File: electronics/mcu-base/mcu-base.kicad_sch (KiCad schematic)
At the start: 1 part

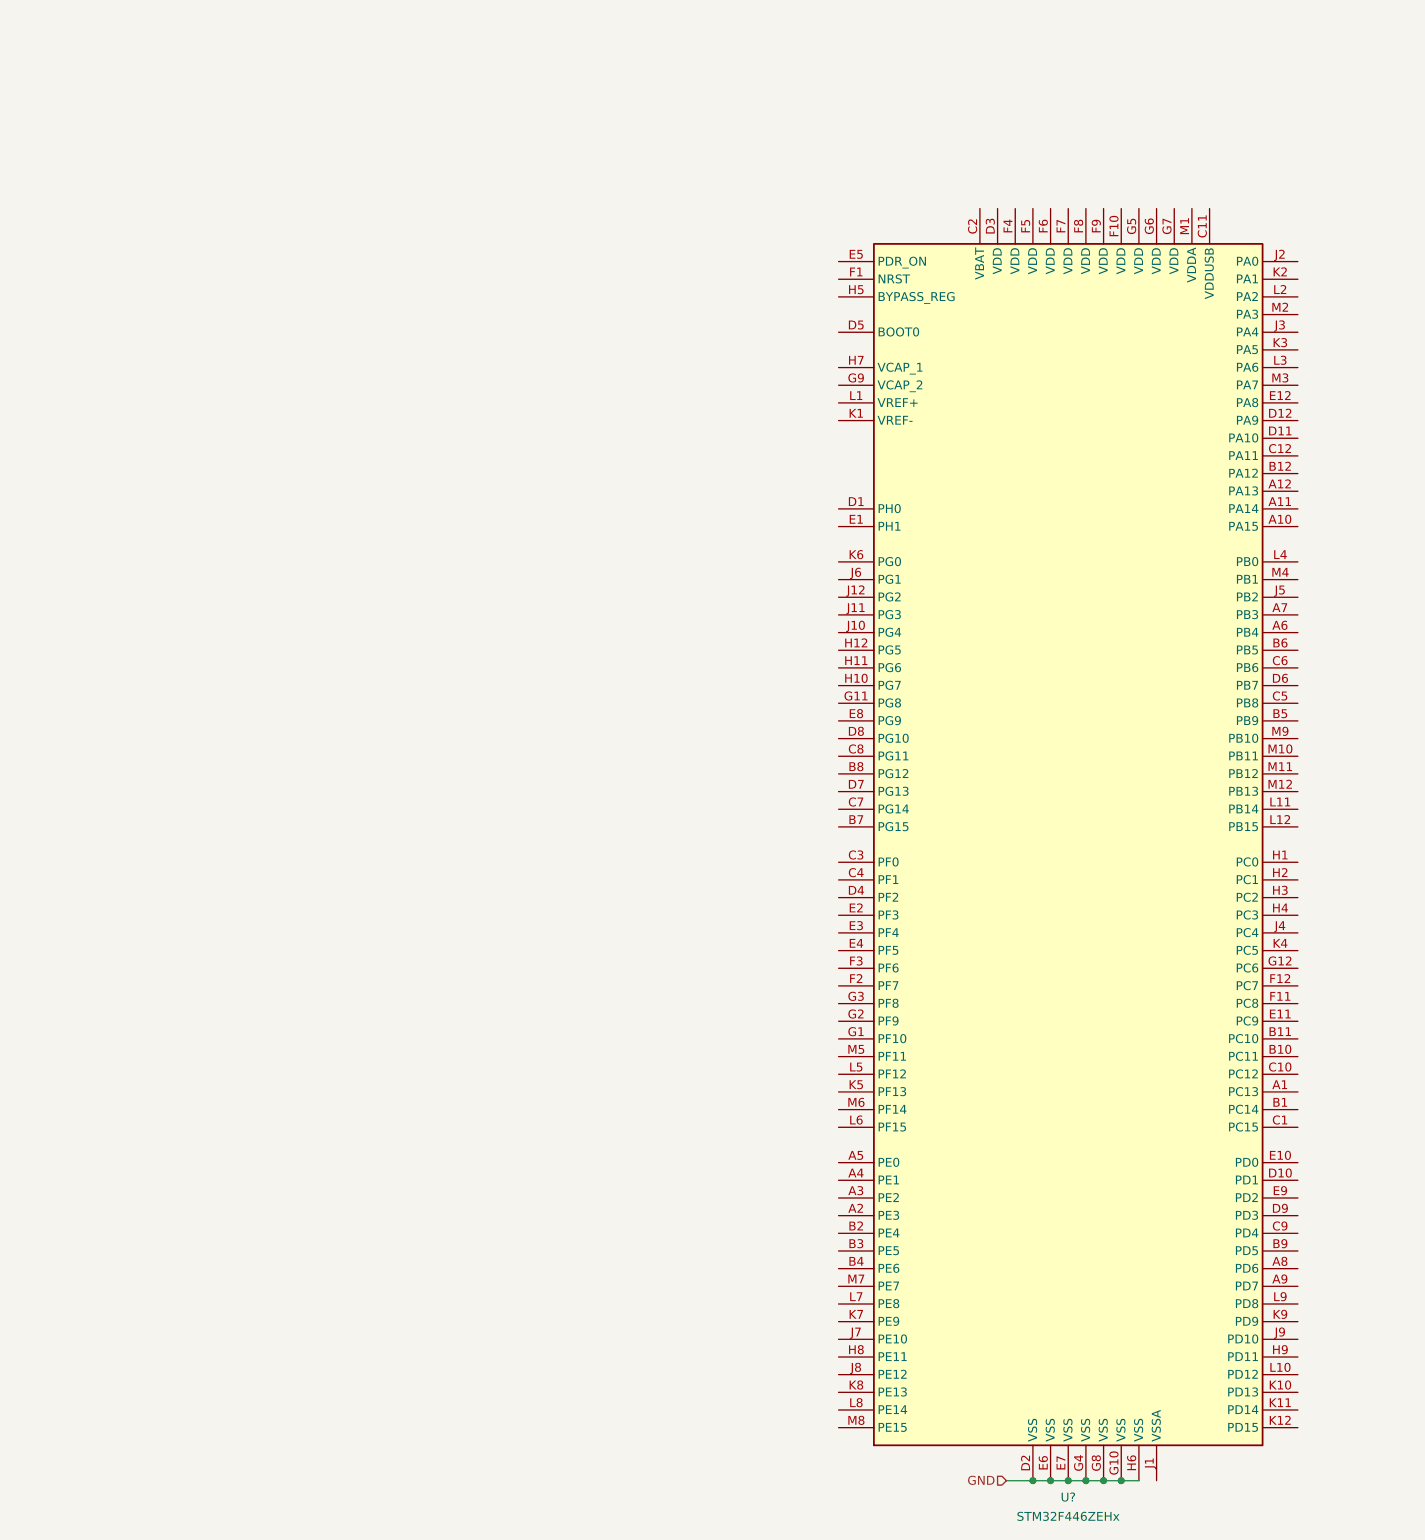
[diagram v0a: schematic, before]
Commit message: Add regulator and CAN transceiver to mcu-base
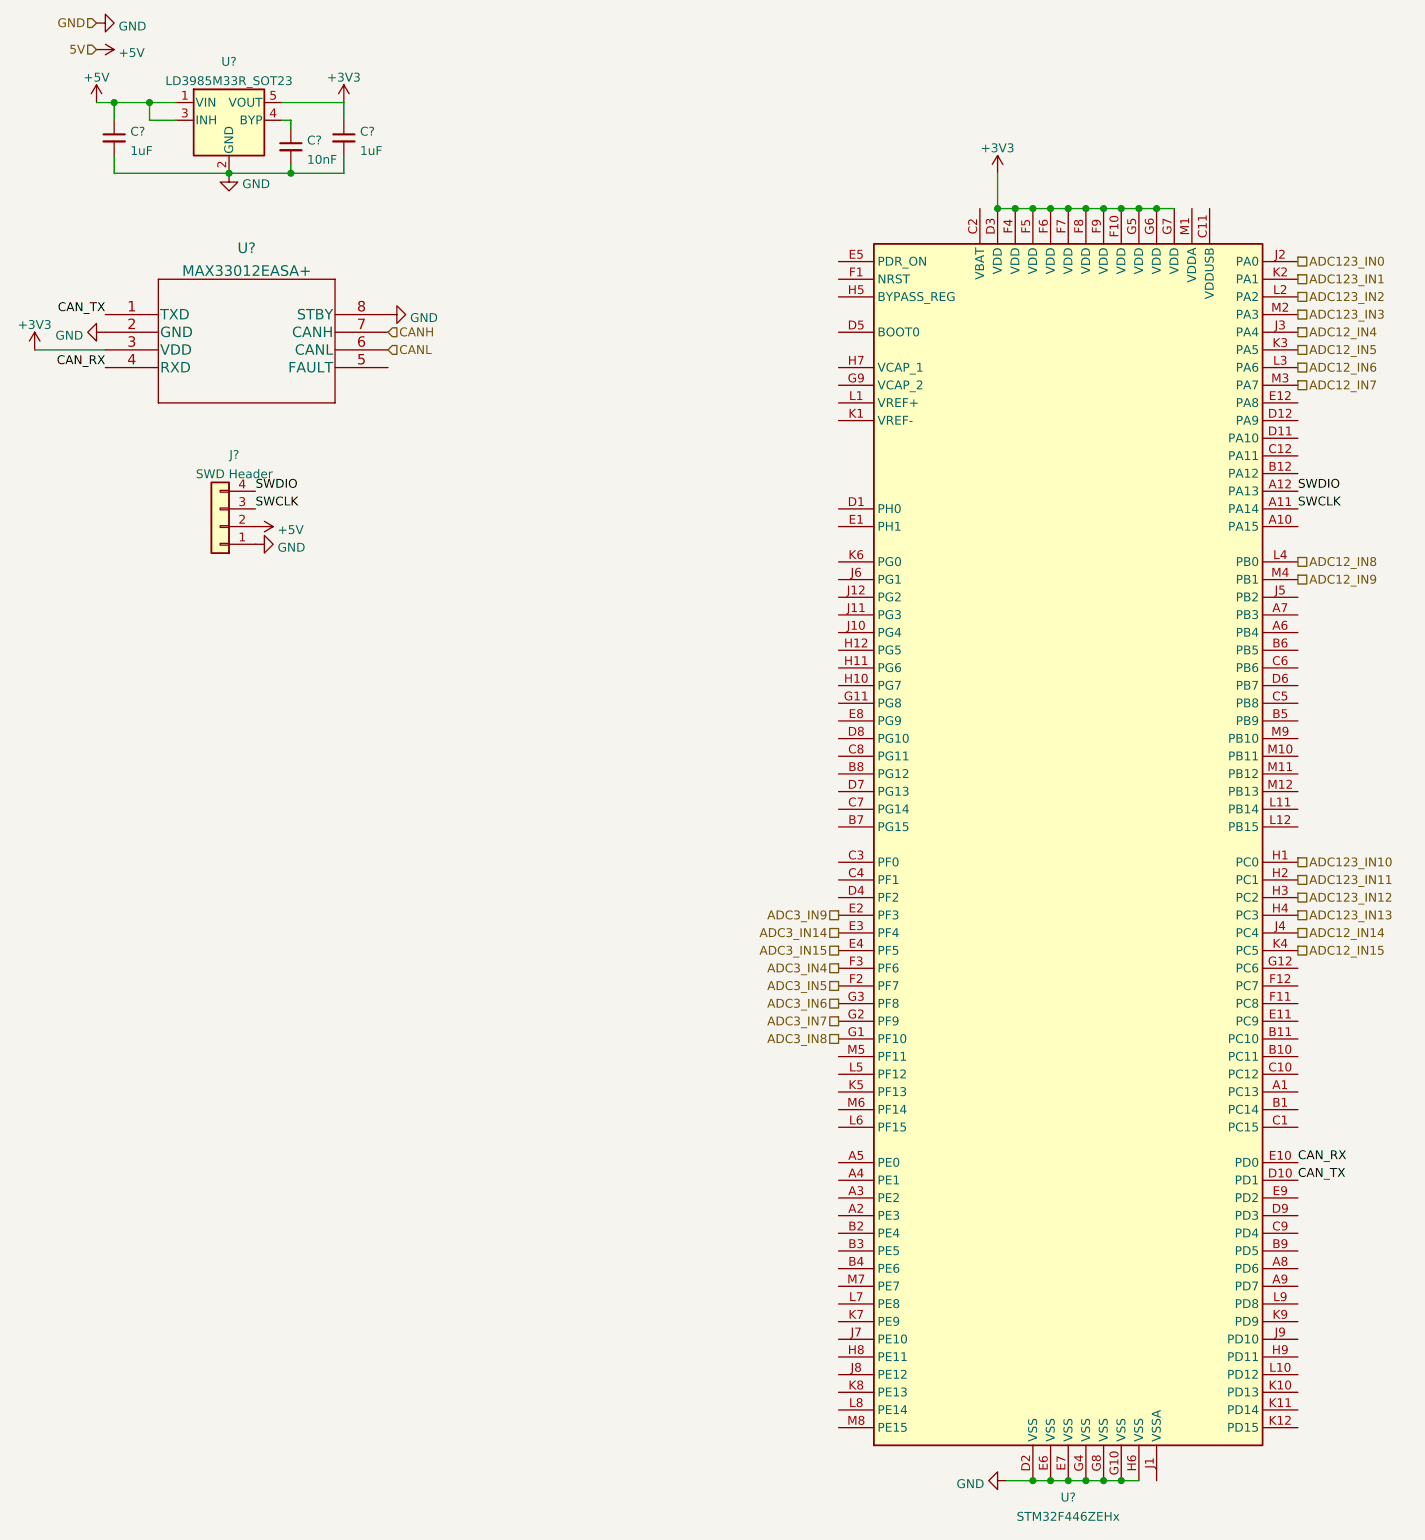
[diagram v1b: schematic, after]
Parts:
- added C? (x2): 1uF, symbol Device:C_Small
- added C?: 10nF, symbol Device:C_Small
- added J?: SWD Header, symbol Connector_Generic:Conn_01x04
- added U?: LD3985M33R_SOT23, Package_TO_SOT_SMD:SOT-23-5, symbol Regulator_Linear:LD3985M33R_SOT23
- added U?: MAX33012EASA+, 21-0041-3-M_90-0096-8L_MXM, symbol MAX33012EASA+:MAX33012EASA+
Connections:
- net GND: now also C?.2, C?.2, C?.2, J?.1 (Pin_1), U?.2 (GND), U?.2 (GND), U?.8 (STBY)
- net SWCLK: now reaches U?.A11 (PA14)
- net SWCLK: now also J?.3 (Pin_3)
- net SWDIO: now reaches U?.A12 (PA13)
- net SWDIO: now also J?.4 (Pin_4)
- net CAN_TX: now reaches U?.D10 (PD1)
- net CAN_TX: now also U?.1 (TXD)
- net +3V3: now reaches U?.D3 (VDD)
- net +3V3: now also U?.F10 (VDD), U?.F4 (VDD), U?.F5 (VDD), U?.F6 (VDD), U?.F7 (VDD), U?.F8 (VDD), U?.F9 (VDD), U?.G5 (VDD), U?.G6 (VDD), U?.G7 (VDD), C?.1, U?.3 (VDD), U?.5 (VOUT)
- net CAN_RX: now reaches U?.E10 (PD0)
- net CAN_RX: now also U?.4 (RXD)
- net ADC3_IN9: now reaches U?.E2 (PF3)
- net ADC3_IN14: now reaches U?.E3 (PF4)
- net ADC3_IN15: now reaches U?.E4 (PF5)
- net ADC3_IN5: now reaches U?.F2 (PF7)
- net ADC3_IN4: now reaches U?.F3 (PF6)
- net ADC3_IN8: now reaches U?.G1 (PF10)
- net ADC3_IN7: now reaches U?.G2 (PF9)
- net ADC3_IN6: now reaches U?.G3 (PF8)
- net ADC123_IN10: now reaches U?.H1 (PC0)
- net ADC123_IN11: now reaches U?.H2 (PC1)
- net ADC123_IN12: now reaches U?.H3 (PC2)
- net ADC123_IN13: now reaches U?.H4 (PC3)
- net ADC123_IN0: now reaches U?.J2 (PA0)
- net ADC12_IN4: now reaches U?.J3 (PA4)
- net ADC12_IN14: now reaches U?.J4 (PC4)
- net ADC123_IN1: now reaches U?.K2 (PA1)
- net ADC12_IN5: now reaches U?.K3 (PA5)
- net ADC12_IN15: now reaches U?.K4 (PC5)
- net ADC123_IN2: now reaches U?.L2 (PA2)
- net ADC12_IN6: now reaches U?.L3 (PA6)
- net ADC12_IN8: now reaches U?.L4 (PB0)
- net ADC123_IN3: now reaches U?.M2 (PA3)
- net ADC12_IN7: now reaches U?.M3 (PA7)
- net ADC12_IN9: now reaches U?.M4 (PB1)
- new net: C?.1, U?.4 (BYP)
- new net +5V: C?.1, J?.2 (Pin_2), U?.1 (VIN), U?.3 (INH)
- new net CANH: U?.7 (CANH)
- new net CANL: U?.6 (CANL)
